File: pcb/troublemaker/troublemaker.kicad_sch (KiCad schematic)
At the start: 116 parts, among them IC1 TEENSY_4.1, J1 neopixel_data_RPI19_GPIO10, J2 taptempo_led_RPI16_GPIO23, J3 5V_RPI2_OR_4, J4 GND_RPI34, J5 Conn_01x12, SW1 sw_eq2, SW10 sw_grain_playback, SW11 btn_sampler_stop, SW2 sw_eq1, SW3 sw_sub, SW4 sw_bass, SW5 sw_mid, SW6 sw_high, SW7 btn_delay_taptempo, SW8 sw_delay_type, SW9 sw_grain_type, U1 RASPBERRY_PI_4B_4GB, U2 CD74HC4067M, U3 CD74HC4067M, U4 CD74HC4067M, U5 CD74HC4067M, U6 CD74HC4067M

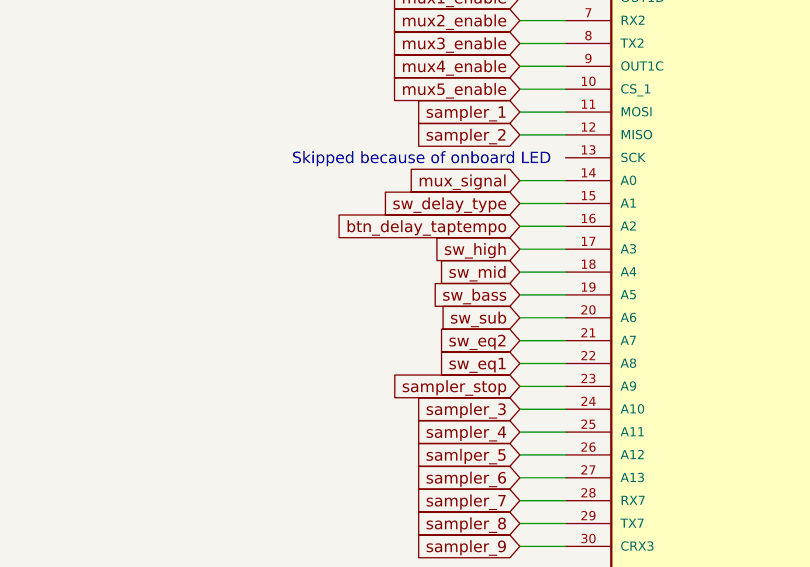
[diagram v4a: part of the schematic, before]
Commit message: All connections done
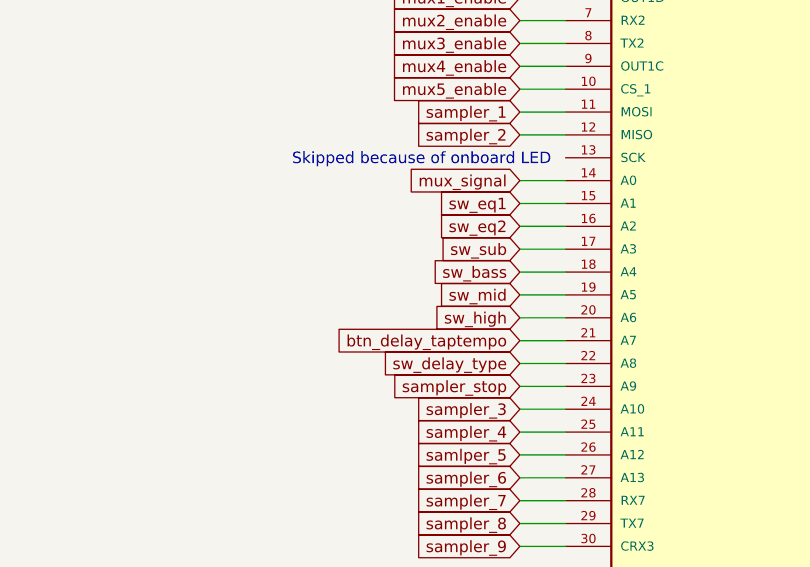
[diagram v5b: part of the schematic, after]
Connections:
- net btn_delay_taptempo: now also IC1.21 (A7); no longer IC1.16 (A2)
- net sw_bass: now also IC1.18 (A4); no longer IC1.19 (A5)
- net sw_delay_type: now also IC1.22 (A8); no longer IC1.15 (A1)
- net sw_eq1: now also IC1.15 (A1); no longer IC1.22 (A8)
- net sw_eq2: now also IC1.16 (A2); no longer IC1.21 (A7)
- net sw_high: now also IC1.20 (A6); no longer IC1.17 (A3)
- net sw_mid: now also IC1.19 (A5); no longer IC1.18 (A4)
- net sw_sub: now also IC1.17 (A3); no longer IC1.20 (A6)
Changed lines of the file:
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@@
 	(wire
 		(pts
-			(xy 124.46 527.05) (xy 129.54 527.05)
-		)
-		(stroke
-			(width 0)
-			(type default)
-		)
-	)
-	(wire
-		(pts
 			(xy 472.44 302.26) (xy 472.44 321.31)
 		)
@@
 	(wire
 		(pts
-			(xy 574.04 299.72) (xy 574.04 248.92)
+			(xy 124.46 529.59) (xy 129.54 529.59)
 		)
 		(stroke
@@
 	(wire
 		(pts
-			(xy 422.91 405.13) (xy 539.115 405.13)
+			(xy 574.04 299.72) (xy 574.04 248.92)
 		)
 		(stroke
@@
 	(wire
 		(pts
-			(xy 306.07 207.01) (xy 449.58 207.01)
+			(xy 422.91 405.13) (xy 539.115 405.13)
 		)
 		(stroke
@@
 	(wire
 		(pts
-			(xy 478.79 312.42) (xy 576.58 312.42)
+			(xy 306.07 207.01) (xy 449.58 207.01)
 		)
 		(stroke
@@
 	(wire
 		(pts
-			(xy 591.185 381.635) (xy 611.505 381.635)
+			(xy 478.79 312.42) (xy 576.58 312.42)
 		)
 		(stroke
@@
 	(wire
 		(pts
-			(xy 279.4 175.26) (xy 293.37 175.26)
+			(xy 591.185 381.635) (xy 611.505 381.635)
 		)
 		(stroke
@@
 	(wire
 		(pts
-			(xy 721.36 204.47) (xy 721.36 200.66)
+			(xy 279.4 175.26) (xy 293.37 175.26)
 		)
 		(stroke
@@
 	(wire
 		(pts
-			(xy 124.46 521.97) (xy 129.54 521.97)
+			(xy 721.36 204.47) (xy 721.36 200.66)
 		)
 		(stroke
@@
 	(wire
 		(pts
+			(xy 124.46 521.97) (xy 129.54 521.97)
+		)
+		(stroke
+			(width 0)
+			(type default)
+		)
+	)
+	(wire
+		(pts
 			(xy 403.86 469.9) (xy 403.86 474.98)
 		)
@@
 	(wire
 		(pts
-			(xy 124.46 534.67) (xy 129.54 534.67)
-		)
-		(stroke
-			(width 0)
-			(type default)
-		)
-	)
-	(wire
-		(pts
 			(xy 124.46 542.29) (xy 129.54 542.29)
 		)
@@
 	(wire
 		(pts
+			(xy 124.46 532.13) (xy 129.54 532.13)
+		)
+		(stroke
+			(width 0)
+			(type default)
+		)
+	)
+	(wire
+		(pts
 			(xy 114.3 115.57) (xy 81.28 115.57)
 		)
@@
 	(wire
 		(pts
+			(xy 124.46 527.05) (xy 129.54 527.05)
+		)
+		(stroke
+			(width 0)
+			(type default)
+		)
+	)
+	(wire
+		(pts
 			(xy 619.76 166.37) (xy 619.76 203.2)
 		)
@@
 	(wire
 		(pts
-			(xy 124.46 539.75) (xy 129.54 539.75)
-		)
-		(stroke
-			(width 0)
-			(type default)
-		)
-	)
-	(wire
-		(pts
 			(xy 692.15 168.91) (xy 708.66 168.91)
 		)
@@
 	(wire
 		(pts
+			(xy 124.46 539.75) (xy 129.54 539.75)
+		)
+		(stroke
+			(width 0)
+			(type default)
+		)
+	)
+	(wire
+		(pts
 			(xy 632.46 168.91) (xy 650.24 168.91)
 		)
@@
 	(wire
 		(pts
-			(xy 532.13 444.5) (xy 551.18 444.5)
+			(xy 124.46 537.21) (xy 129.54 537.21)
 		)
 		(stroke
@@
 	(wire
 		(pts
-			(xy 430.53 204.47) (xy 430.53 226.06)
+			(xy 532.13 444.5) (xy 551.18 444.5)
 		)
 		(stroke
@@
 	(wire
 		(pts
-			(xy 671.83 287.02) (xy 671.83 299.72)
+			(xy 430.53 204.47) (xy 430.53 226.06)
 		)
 		(stroke
@@
 	(wire
 		(pts
-			(xy 124.46 547.37) (xy 129.54 547.37)
+			(xy 671.83 287.02) (xy 671.83 299.72)
 		)
 		(stroke
@@
 	(wire
 		(pts
-			(xy 494.03 295.91) (xy 497.84 295.91)
+			(xy 124.46 547.37) (xy 129.54 547.37)
 		)
 		(stroke
@@
 	(wire
 		(pts
-			(xy 124.46 509.27) (xy 129.54 509.27)
+			(xy 494.03 295.91) (xy 497.84 295.91)
 		)
 		(stroke
@@
 	(wire
 		(pts
-			(xy 445.77 231.14) (xy 467.36 231.14)
+			(xy 124.46 509.27) (xy 129.54 509.27)
 		)
 		(stroke
@@
 	(wire
 		(pts
-			(xy 124.46 524.51) (xy 129.54 524.51)
+			(xy 445.77 231.14) (xy 467.36 231.14)
 		)
 		(stroke
@@
 	(wire
 		(pts
+			(xy 124.46 524.51) (xy 129.54 524.51)
+		)
+		(stroke
+			(width 0)
+			(type default)
+		)
+	)
+	(wire
+		(pts
 			(xy 411.48 135.89) (xy 411.48 177.8)
 		)
@@
 	(wire
 		(pts
-			(xy 124.46 532.13) (xy 129.54 532.13)
-		)
-		(stroke
-			(width 0)
-			(type default)
-		)
-	)
-	(wire
-		(pts
 			(xy 737.87 166.37) (xy 737.87 203.2)
 		)
@@
 	(wire
 		(pts
-			(xy 124.46 529.59) (xy 129.54 529.59)
-		)
-		(stroke
-			(width 0)
-			(type default)
-		)
-	)
-	(wire
-		(pts
 			(xy 551.18 444.5) (xy 570.23 444.5)
 		)
@@
 	(wire
 		(pts
-			(xy 124.46 537.21) (xy 129.54 537.21)
-		)
-		(stroke
-			(width 0)
-			(type default)
-		)
-	)
-	(wire
-		(pts
 			(xy 570.23 537.21) (xy 589.28 537.21)
 		)
@@
 	(wire
 		(pts
+			(xy 124.46 534.67) (xy 129.54 534.67)
+		)
+		(stroke
+			(width 0)
+			(type default)
+		)
+	)
+	(wire
+		(pts
 			(xy 767.08 168.91) (xy 767.08 205.74)
 		)
@@
 	(global_label "sw_high"
 		(shape input)
-		(at 124.46 527.05 180)
+		(at 124.46 534.67 180)
 		(fields_autoplaced yes)
 		(effects
@@
 		)
 		(property "Intersheetrefs" "${INTERSHEET_REFS}"
-			(at 114.0968 527.05 0)
+			(at 114.0968 534.67 0)
 			(effects
 				(font
@@
 	(global_label "sw_bass"
 		(shape input)
-		(at 124.46 532.13 180)
+		(at 124.46 529.59 180)
 		(fields_autoplaced yes)
 		(effects
@@
 		)
 		(property "Intersheetrefs" "${INTERSHEET_REFS}"
-			(at 113.7944 532.13 0)
+			(at 113.7944 529.59 0)
 			(effects
 				(font
@@
 	(global_label "sw_eq1"
 		(shape input)
-		(at 124.46 539.75 180)
+		(at 124.46 521.97 180)
 		(fields_autoplaced yes)
 		(effects
@@
 		)
 		(property "Intersheetrefs" "${INTERSHEET_REFS}"
-			(at 114.7015 539.75 0)
+			(at 114.7015 521.97 0)
 			(effects
 				(font
@@
 	(global_label "btn_delay_taptempo"
 		(shape input)
-		(at 124.46 524.51 180)
+		(at 124.46 537.21 180)
 		(fields_autoplaced yes)
 		(effects
@@
 		)
 		(property "Intersheetrefs" "${INTERSHEET_REFS}"
-			(at 102.6672 524.51 0)
+			(at 102.6672 537.21 0)
 			(effects
 				(font
@@
 	(global_label "sw_mid"
 		(shape input)
-		(at 124.46 529.59 180)
+		(at 124.46 532.13 180)
 		(fields_autoplaced yes)
 		(effects
@@
 		)
 		(property "Intersheetrefs" "${INTERSHEET_REFS}"
-			(at 114.7015 529.59 0)
+			(at 114.7015 532.13 0)
 			(effects
 				(font
@@
 	(global_label "sw_delay_type"
 		(shape input)
-		(at 124.46 521.97 180)
+		(at 124.46 539.75 180)
 		(fields_autoplaced yes)
 		(effects
@@
 		)
 		(property "Intersheetrefs" "${INTERSHEET_REFS}"
-			(at 108.2307 521.97 0)
+			(at 108.2307 539.75 0)
 			(effects
 				(font
@@
 	(global_label "sw_eq2"
 		(shape input)
-		(at 124.46 537.21 180)
+		(at 124.46 524.51 180)
 		(fields_autoplaced yes)
 		(effects
@@
 		)
 		(property "Intersheetrefs" "${INTERSHEET_REFS}"
-			(at 114.7015 537.21 0)
+			(at 114.7015 524.51 0)
 			(effects
 				(font
@@
 	(global_label "sw_sub"
 		(shape input)
-		(at 124.46 534.67 180)
+		(at 124.46 527.05 180)
 		(fields_autoplaced yes)
 		(effects
@@
 		)
 		(property "Intersheetrefs" "${INTERSHEET_REFS}"
-			(at 114.8225 534.67 0)
+			(at 114.8225 527.05 0)
 			(effects
 				(font

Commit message: Removed capacitors as I already have them on the breakout board. Small reroutes.
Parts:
- removed C1, C2, C3, C4, C5: C_Small, Capacitor_THT:CP_Radial_D5.0mm_P2.00mm, symbol Library:C_Small

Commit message: added expansion port and GPIO socket
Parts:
- removed J1: neopixel_data_RPI19_GPIO10, Connector_PinHeader_1.00mm:PinHeader_1x01_P1.00mm_Vertical, symbol Library:Conn_01x01
- removed J2: taptempo_led_RPI16_GPIO23, Connector_PinHeader_1.00mm:PinHeader_1x01_P1.00mm_Vertical, symbol Library:Conn_01x01
- added J1: RPi_GPIO, Connector_IDC:IDC-Header_2x20_P2.54mm_Vertical, symbol Connector_Generic:Conn_02x20_Odd_Even
- added J25: EXPANSION_PORT, Connector_IDC:IDC-Header_2x17_P2.54mm_Vertical, symbol Connector_Generic:Conn_02x17_Odd_Even
- added SW12: sw_input_mode, Library:SW_SPDT_red_leozor, symbol Library:SW_SPDT
- Neopixel_bass_gain_reduction1, Neopixel_bass_out_level1, Neopixel_high_gain_reduction1, Neopixel_high_out_level1, Neopixel_mid_gain_reduction1, Neopixel_mid_out_level1, Neopixel_sub_gain_reduction1, Neopixel_sub_out_level1: footprint leozorLib:Neopixel-8LED -> Library:Neopixel-8LED
- SW1, SW10, SW2, SW3, SW4, SW5, SW6, SW8, SW9: footprint leozorLib:SW_SPDT_red_leozor -> Library:SW_SPDT_red_leozor
- SW11, SW7: footprint leozorLib:arcade_service_button_leozor -> Library:arcade_service_button_leozor
- U2, U3, U4, U5, U6: footprint leozorLib:Breakout_HC4067_PTH_Only -> Library:Breakout_HC4067_PTH_Only
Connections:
- net +5V: now also J1.2 (Pin_2), J1.4 (Pin_4), J25.6 (Pin_6)
- net 3v3: now also J25.8 (Pin_8)
- net GND: now also J1.14 (Pin_14), J1.20 (Pin_20), J1.25 (Pin_25), J1.30 (Pin_30), J1.34 (Pin_34), J1.39 (Pin_39), J1.6 (Pin_6), J1.9 (Pin_9), J25.2 (Pin_2), J25.4 (Pin_4), SW12.2 (B)
- net mux_s0: now also J25.1 (Pin_1)
- net mux_s1: now also J25.3 (Pin_3)
- net mux_s2: now also J25.5 (Pin_5)
- net mux_s3: now also J25.7 (Pin_7)
- net mux_signal: now also J25.9 (Pin_9)
- net neopixel_data: now also J1.19 (Pin_19)
- net XT_Teensy33: now reaches IC1.33 (MCLK2)
- net XT_Teensy33: now also J25.22 (Pin_22)
- net XT_Teensy34: now reaches IC1.34 (RX8)
- net XT_Teensy34: now also J25.20 (Pin_20)
- net XT_Teensy35: now reaches IC1.35 (TX8)
- net XT_Teensy35: now also J25.18 (Pin_18)
- net XT_Teensy36: now reaches IC1.36 (CS_2)
- net XT_Teensy36: now also J25.16 (Pin_16)
- net XT_Teensy37: now reaches IC1.37 (CS_3)
- net XT_Teensy37: now also J25.14 (Pin_14)
- net XT_Teensy40: now reaches IC1.40 (A16)
- net XT_Teensy40: now also J25.12 (Pin_12)
- net XT_Teensy41: now reaches IC1.41 (A17)
- net XT_Teensy41: now also J25.10 (Pin_10)
- net taptempo_LED renamed taptempo_LED_RPi16
- net taptempo_LED_RPi16: now also J1.16 (Pin_16)
- new net XT_RPi10: J1.10 (Pin_10), J25.21 (Pin_21)
- new net XT_RPi11: J1.11 (Pin_11), J25.27 (Pin_27)
- new net XT_RPi13: J1.13 (Pin_13), J25.29 (Pin_29)
- new net XT_RPi15: J1.15 (Pin_15), J25.31 (Pin_31)
- new net XT_RPi18: J1.18 (Pin_18), J25.33 (Pin_33)
- new net XT_RPi22: J25.34 (Pin_34)
- new net XT_RPi23: J1.23 (Pin_23), J25.28 (Pin_28)
- new net XT_RPi24: J25.32 (Pin_32)
- new net XT_RPi26: J25.30 (Pin_30)
- new net XT_RPi29: J1.29 (Pin_29), J25.19 (Pin_19)
- new net XT_RPi31: J1.31 (Pin_31), J25.17 (Pin_17)
- new net XT_RPi32: J1.32 (Pin_32), J25.15 (Pin_15)
- new net XT_RPi33: J1.33 (Pin_33), J25.13 (Pin_13)
- new net XT_RPi36: J1.36 (Pin_36), J25.11 (Pin_11)
- new net XT_RPi37: J1.37 (Pin_37), J25.24 (Pin_24)
- new net XT_RPi7: J1.7 (Pin_7), J25.25 (Pin_25)
- new net XT_RPi8: J1.8 (Pin_8), J25.23 (Pin_23)
- new net sw_input_mode_RPi21: J1.21 (Pin_21), J25.26 (Pin_26), SW12.1 (A)
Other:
- note added: "HIFIBERRY"
- note added: "Reserved"
- note added: "Unused"

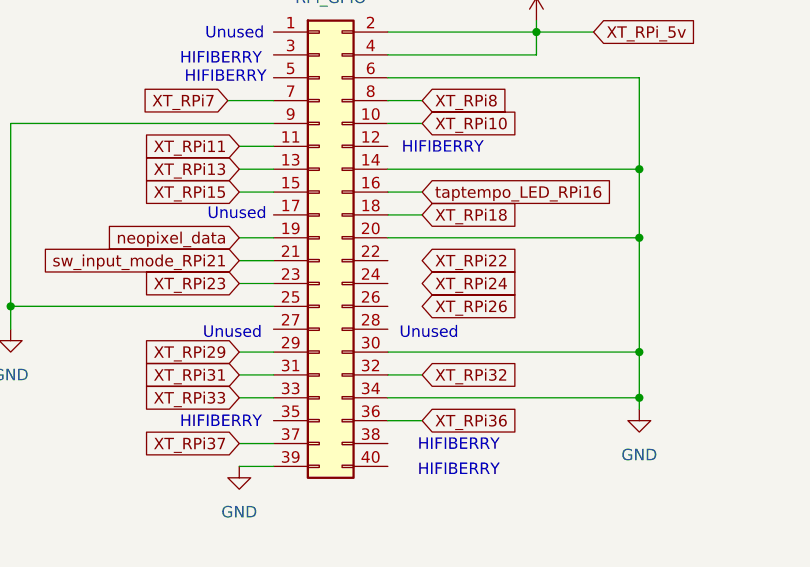
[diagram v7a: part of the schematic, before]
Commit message: added mooncrown logo
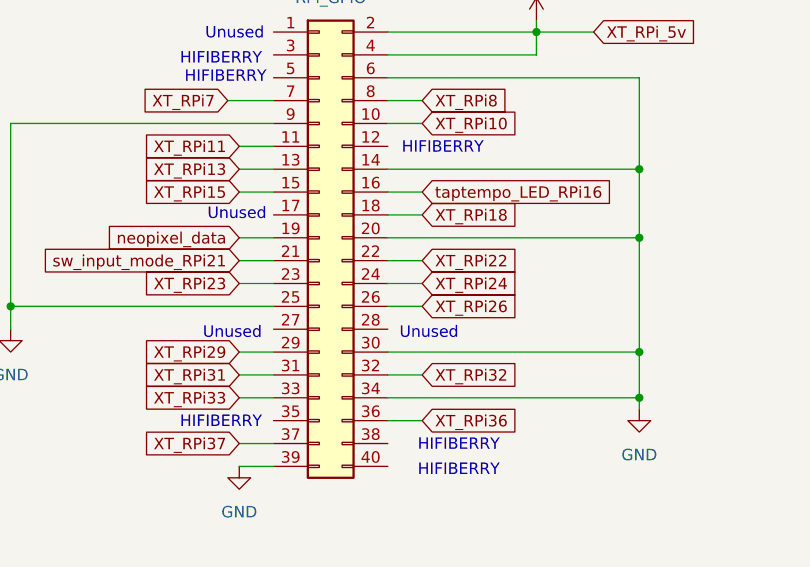
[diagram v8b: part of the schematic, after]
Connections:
- net XT_RPi22: now also J1.22 (Pin_22)
- net XT_RPi24: now also J1.24 (Pin_24)
- net XT_RPi26: now also J1.26 (Pin_26)
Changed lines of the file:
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@@
 	(wire
 		(pts
+			(xy 314.96 450.85) (xy 318.77 450.85)
+		)
+		(stroke
+			(width 0)
+			(type default)
+		)
+	)
+	(wire
+		(pts
 			(xy 742.95 360.68) (xy 746.76 360.68)
 		)
@@
 	(wire
 		(pts
+			(xy 314.96 448.31) (xy 318.77 448.31)
+		)
+		(stroke
+			(width 0)
+			(type default)
+		)
+	)
+	(wire
+		(pts
 			(xy 476.25 297.18) (xy 476.25 317.5)
 		)
@@
 		)
 		(stroke
+			(width 0)
+			(type default)
+		)
+	)
+	(wire
+		(pts
+			(xy 314.96 445.77) (xy 318.77 445.77)
+		)
+		(stroke
